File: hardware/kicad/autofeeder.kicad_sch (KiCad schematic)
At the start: 41 parts, among them J1 BATTERY, J2 MOTOR, J3 USB-C, J4 PROG, SW1_POWER1 Alps SKRPADE010, SW2_TIMER1 Alps SKRPADE010, SW3_MANUAL1 Alps SKRPADE010, SW4_SETTINGS1 Alps SKRPADE010, SW5_UP1 Alps SKRPADE010, SW6_DOWN1 Alps SKRPADE010, U1 ESP32-C6-WROOM-1, U2 TP4056, U3 DW01A+FS8205A, U4 TPS63802, U5 DRV8871, U6 SN65HVD230

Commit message: Snapshot current design (ESP32-C6-Zero, RT6150A buck-boost, FS8205A protection)
- Switch from ESP32-C6-WROOM module to Waveshare ESP32-C6-Zero (socketed)
- Replace TPS63802 (QFN) with RT6150A (SOT-23-6, hand-solderable)
- Split DW01A+FS8205A into separate U3/U8 symbols (SOT-23-6)
- Add gerber/drill/CPL fabrication output
- Add mounting holes and OLED SPI display footprint
- Generate schematic + PCB from Python pipeline scripts
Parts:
- removed GND_MAIN1: GND, symbol power:GND
- removed LED_STATUS1: GREEN, LED_SMD:LED_0603_1608Metric, symbol Device:LED
- removed PWR_3V3, PWR_BATT1, PWR_VBUS1: PWR_FLAG, symbol power:PWR_FLAG
- removed R7: 330R, Resistor_SMD:R_0603_1608Metric, symbol Device:R
- removed R9: 10k, Resistor_SMD:R_0603_1608Metric, symbol Device:R
- added L1: 4.7uH, Inductor_SMD:L_0805_2012Metric, symbol Device:L
- added R11: 470k, Resistor_SMD:R_0603_1608Metric, symbol Device:R
- added R12: 100k, Resistor_SMD:R_0603_1608Metric, symbol Device:R
- added R13: 10k, Resistor_SMD:R_0603_1608Metric, symbol Device:R
- added U8: FS8205A, Package_TO_SOT_SMD:SOT-23-6_Handsoldering, symbol autofeeder:FS8205A
- DISP1: footprint Display:SSD1306_128x64_SPI -> autofeeder:OLED_1.3in_SSD1306_SPI
- J4: value PROG -> DBG
- SW1_POWER1, SW2_TIMER1, SW3_MANUAL1, SW4_SETTINGS1, SW5_UP1, SW6_DOWN1: footprint Button_Switch_SMD:SW_SPST_SKRPADE010 -> Button_Switch_SMD:SW_Push_1P1T_NO_CK_KMR2
- U1: value ESP32-C6-WROOM-1 -> ESP32-C6-Zero; footprint (none) -> autofeeder:ESP32_C6_Zero; symbol autofeeder:ESP32-C6-WROOM-1 -> autofeeder:ESP32_C6_Zero
- U3: value DW01A+FS8205A -> DW01A; footprint (none) -> Package_TO_SOT_SMD:SOT-23-6_Handsoldering; symbol autofeeder:DW01A_FS8205A -> Battery_Management:DW01A
- U4: value TPS63802 -> RT6150A; footprint (none) -> Package_TO_SOT_SMD:SOT-23-6_Handsoldering; symbol autofeeder:TPS63802 -> autofeeder:RT6150A
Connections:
- net BATT_CHG: now also U2.5 (BAT), U3.5 (VCC)
- net BATT_N: now also D1.2 (A), J1.2 (Pin2), U3.2 (CS), U3.6 (GND), U8.2 (S1/D2), U8.3 (D1)
- net BATT_P: now also F1.1, J1.1 (Pin1)
- net BATT_PROT: now also C4.1, D1.1 (K), F1.2, R3.1, U4.5 (VIN), U4.6 (VIN2), U5.6 (VM)
- net BAT_MON: now also R3.2, R4.1, U1.16 (GP20)
- net BUTTON_DOWN: now also SW6_DOWN1.1 (P1), U1.9 (GP5)
- net BUTTON_MANUAL: now also SW3_MANUAL1.1 (P1), U1.6 (GP2)
- net BUTTON_POWER: now also SW1_POWER1.1 (P1), U1.4 (GP0)
- net BUTTON_SETTINGS: now also SW4_SETTINGS1.1 (P1), U1.7 (GP3)
- net BUTTON_TIMER: now also SW2_TIMER1.1 (P1), U1.5 (GP1)
- net BUTTON_UP: now also SW5_UP1.1 (P1), U1.8 (GP4)
- net CAN_H: now also J3.A8 (SBU1), R5.1, R6.1, R6.2, U6.7 (CANH)
- net CAN_L: now also J3.B8 (SBU2), R10.1, R10.2, R5.2, U6.6 (CANL)
- net CAN_RX: now also U1.18 (GP22), U6.4 (R)
- net CAN_TX: now also U1.17 (GP21), U6.1 (D)
- net CC1: now also J3.A5 (CC1), R_CC1.1
- net CC2: now also J3.B5 (CC2), R_CC2.1
- net CHRG_L: now also LED_CHG1.1 (K), U2.1 (CHRG)
- net DISP_CS: now also DISP1.3 (CS), U1.14 (GP18)
- net DISP_DC: now also DISP1.4 (DC), U1.15 (GP19)
- net DISP_MOSI: now also DISP1.7 (MOSI), U1.13 (GP15)
- net DISP_RST: now also DISP1.5 (RST), R13.2
- net DISP_SCK: now also DISP1.6 (SCK), U1.12 (GP14)
- net FB: now also U4.3 (FB), R11.2, R12.1
- net GND: now also C1.2, C2.2, C3.2, C4.2, C5.2, C6.2, DISP1.2 (GND), J3.A1 (GND), J3.A12 (GND), J3.B1 (GND), J3.B12 (GND), J4.4 (Pin_4), LED_CHG1.2 (A), R2_C1.2, R4.2, R_CC1.2, R_CC2.2, SW1_POWER1.2 (P2), SW2_TIMER1.2 (P2), SW3_MANUAL1.2 (P2), SW4_SETTINGS1.2 (P2), SW5_UP1.2 (P2), SW6_DOWN1.2 (P2), U1.2 (GND), U2.3 (GND), U4.2 (GND), U5.5 (GND), U6.2 (GND), R12.2, U8.5 (S2)
- net IPROPI_NC: now also U5.4 (IPROPI)
- net M1_N: now also J2.2 (Pin2), U5.8 (OUT2)
- net M1_P: now also J2.1 (Pin1), U5.7 (OUT1)
- net MOTOR_IN1: now also U1.10 (TX), U5.1 (IN1)
- net MOTOR_IN2: now also U1.11 (RX), U5.2 (IN2)
- net PROG: now also R2_C1.1, U2.2 (PROG)
- net RS_NC: now also U6.8 (Rs)
- net STDBY_L: now also U2.8 (STDBY)
- net SW: now also U4.1 (SW), L1.1
- net TEMP_NC: now also U2.6 (TEMP)
- net VCC_3V3: now also C1.1, C2.1, C3.1, C5.1, C6.1, DISP1.1 (VCC), J4.1 (Pin_1), U1.3 (3V3), U4.4 (EN), U6.3 (VCC), L1.2, R11.1, R13.1
- net VREF_NC: now also U5.3 (VREF), U6.5 (VREF)
- new net NC_TD: U3.4 (TD)
- new net OC_GATE: U3.3 (OC), U8.4 (G2)
- new net OD_GATE: U3.1 (OD), U8.1 (G1)
- new net VBUS: J3.A4 (VBUS), J3.A9 (VBUS), J3.B4 (VBUS), J3.B9 (VBUS), U2.4 (VCC), U2.7 (CE)
- no-connect marks 9 -> 21

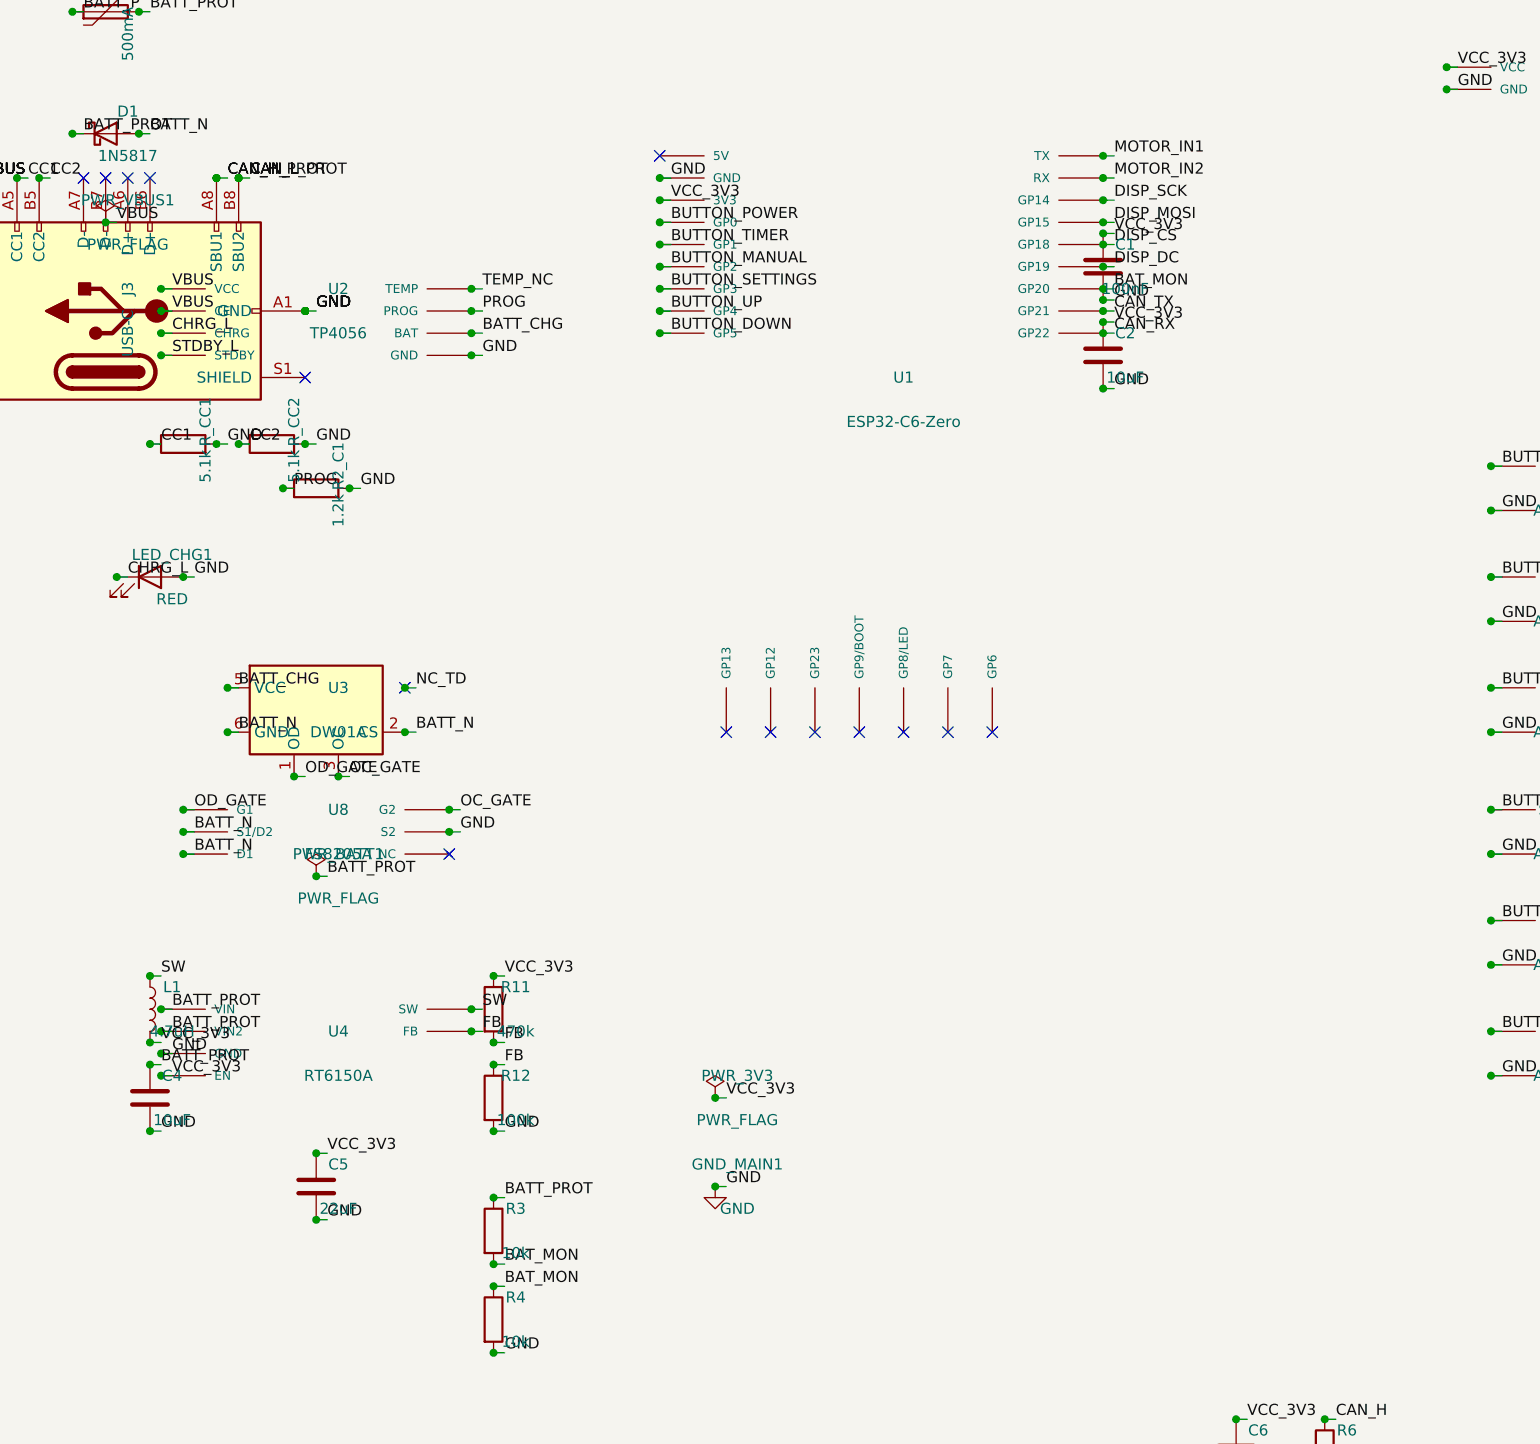
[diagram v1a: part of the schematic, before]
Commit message: Add RTC, GPS, pogo pin support and standalone firmware
- Fix GPIO19/GPIO20 pin conflicts: move DISP_DC to GP12 (bottom pad),
  BAT_MON to GP6 (bottom pad)
- Add J_RTC header: DS3231 RTC module on I2C (GP13/GP23)
- Add J_GPS header: NEO-6M/8M GPS module on UART (GP7/GP8)
- Enlarge bottom edge pads 19-25 to 1.0mm drill for 0.9mm pogo pins
- Rewrite ESPHome firmware: DS3231 RTC time, GPS, 6-page display menu,
  4 persistent schedule slots, button-driven local control
- Update pinout, BOM, and PCB placement for all new components
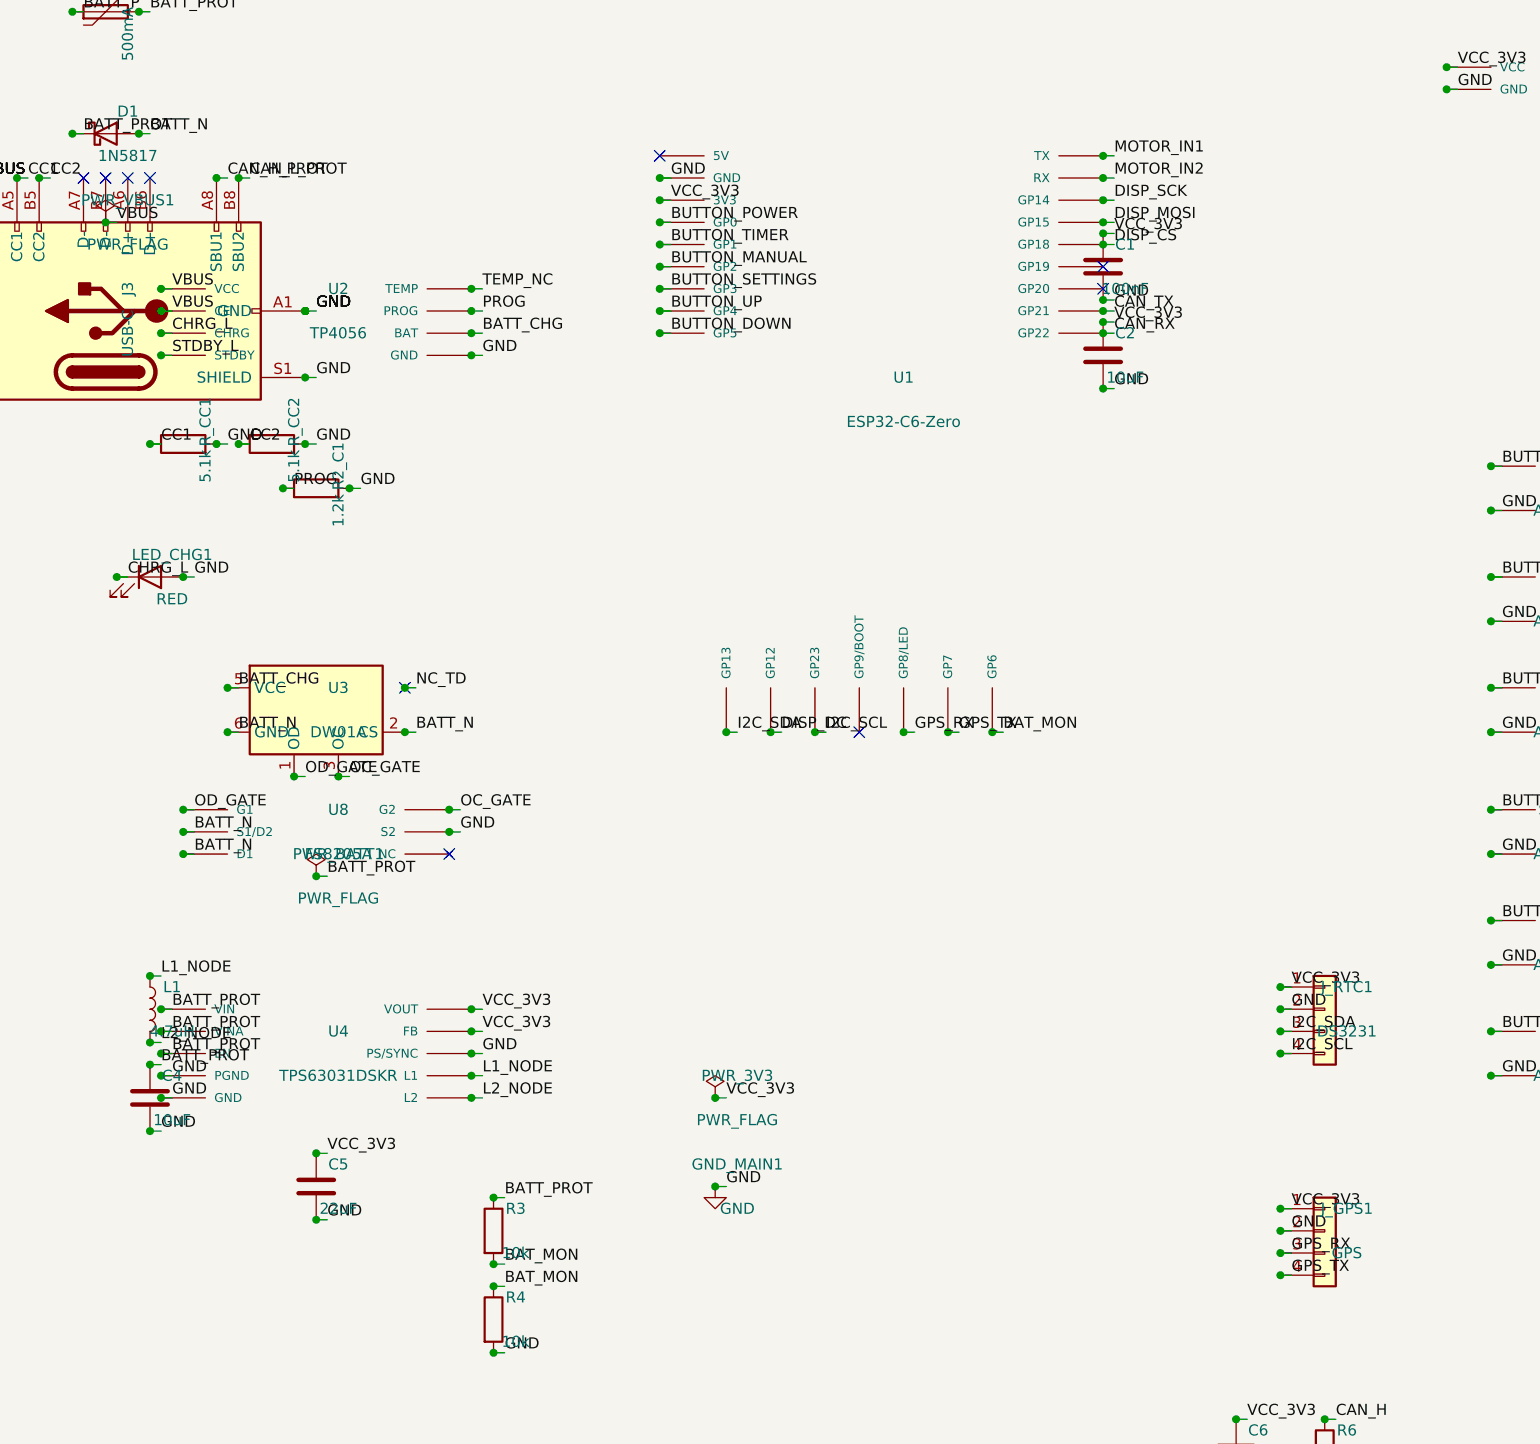
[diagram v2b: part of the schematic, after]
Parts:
- removed R11: 470k, Resistor_SMD:R_0603_1608Metric, symbol Device:R
- removed R12: 100k, Resistor_SMD:R_0603_1608Metric, symbol Device:R
- added J_GPS1: GPS, Connector_PinHeader_2.54mm:PinHeader_1x04_P2.54mm_Vertical, symbol Connector_Generic:Conn_01x04
- added J_RTC1: DS3231, Connector_PinHeader_2.54mm:PinHeader_1x04_P2.54mm_Vertical, symbol Connector_Generic:Conn_01x04
- U4: value RT6150A -> TPS63031DSKR; footprint Package_TO_SOT_SMD:SOT-23-6_Handsoldering -> (none); symbol autofeeder:RT6150A -> autofeeder:TPS63031DSKR
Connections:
- net FB is gone; now on net GND: U4.3 (PGND)
- net BATT_PROT: now also U4.8 (VINA)
- net BAT_MON: now also U1.25 (GP6); no longer U1.16 (GP20)
- net CAN_H: no longer J3.A8 (SBU1), R6.2
- net CAN_L: no longer J3.B8 (SBU2), R10.2
- net DISP_DC: now also U1.20 (GP12); no longer U1.15 (GP19)
- net GND: now also J3.S1 (SHIELD), U4.7 (PS/SYNC), U4.9 (GND), J_GPS1.2 (Pin_2), J_RTC1.2 (Pin_2); no longer U4.2 (GND)
- net VCC_3V3: now also U4.1 (VOUT), U4.10 (FB), J_GPS1.1 (Pin_1), J_RTC1.1 (Pin_1); no longer L1.2, U4.4 (EN)
- net I2C_SDA: now reaches U1.19 (GP13)
- net I2C_SDA: now also J_RTC1.3 (Pin_3)
- net I2C_SCL: now reaches U1.21 (GP23)
- net I2C_SCL: now also J_RTC1.4 (Pin_4)
- net GPS_RX: now reaches U1.23 (GP8/LED)
- net GPS_RX: now also J_GPS1.3 (Pin_3)
- net GPS_TX: now reaches U1.24 (GP7)
- net GPS_TX: now also J_GPS1.4 (Pin_4)
- net SW renamed L1_NODE
- net L1_NODE: now also U4.4 (L1); no longer U4.1 (SW)
- new net CAN_H_PROT: J3.A8 (SBU1), R6.2
- new net CAN_L_PROT: J3.B8 (SBU2), R10.2
- new net L2_NODE: L1.2, U4.2 (L2)
- no-connect marks 21 -> 16

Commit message: Add standalone firmware with RTC, GPS, OLED UI, and menu system
- ESPHome firmware (autofeeder.yaml): RTC timekeeping with DS1307, SNTP+GPS
  fallback, SSD1306 display with clock/manual feed/schedules/GPS/Settings menu,
  6 GPIO buttons, DRV8871 motor control, battery monitoring, CAN bus
- GPS time sync: 30s interval checks TinyGPSPlus, sets system time via
  settimeofday, persists to DS1307 via write_time()
- Hardware: J_RTC at (28,36) back side under OLED, J_GPS at (44,14) top-right,
  U4 TPS63031 WSON-10 footprint fix, bottom pads 19-25 enlarged to 1.0mm for
  0.9mm pogo pins
- Fabrication outputs regenerated (Gerbers, BOM, CPL)
- Docs: pinout.md, bom.md updated for new headers and modules
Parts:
- U4: footprint (none) -> Package_SON:WSON-10-1EP_2.5x2.5mm_P0.5mm_EP1.2x2mm
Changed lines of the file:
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@@
 			)
 		)
-		(property "Footprint" ""
+		(property "Footprint" "Package_SON:WSON-10-1EP_2.5x2.5mm_P0.5mm_EP1.2x2mm"
 			(at 57.15 149.86 0)
 			(effects
